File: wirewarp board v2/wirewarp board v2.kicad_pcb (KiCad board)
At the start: 2 copper layers, 1443 parts

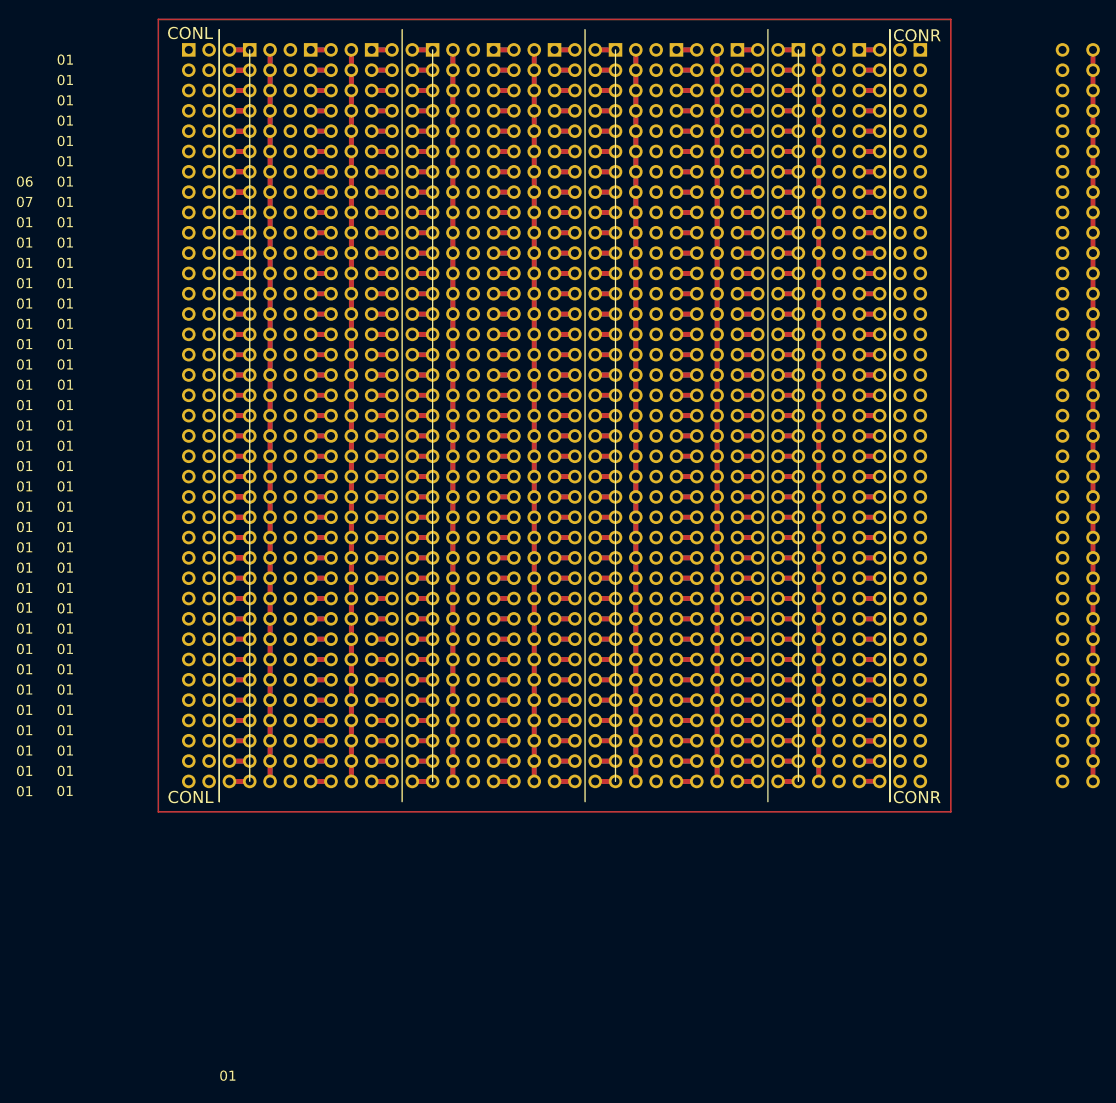
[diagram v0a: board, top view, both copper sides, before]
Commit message: protoboard sketch on kicad
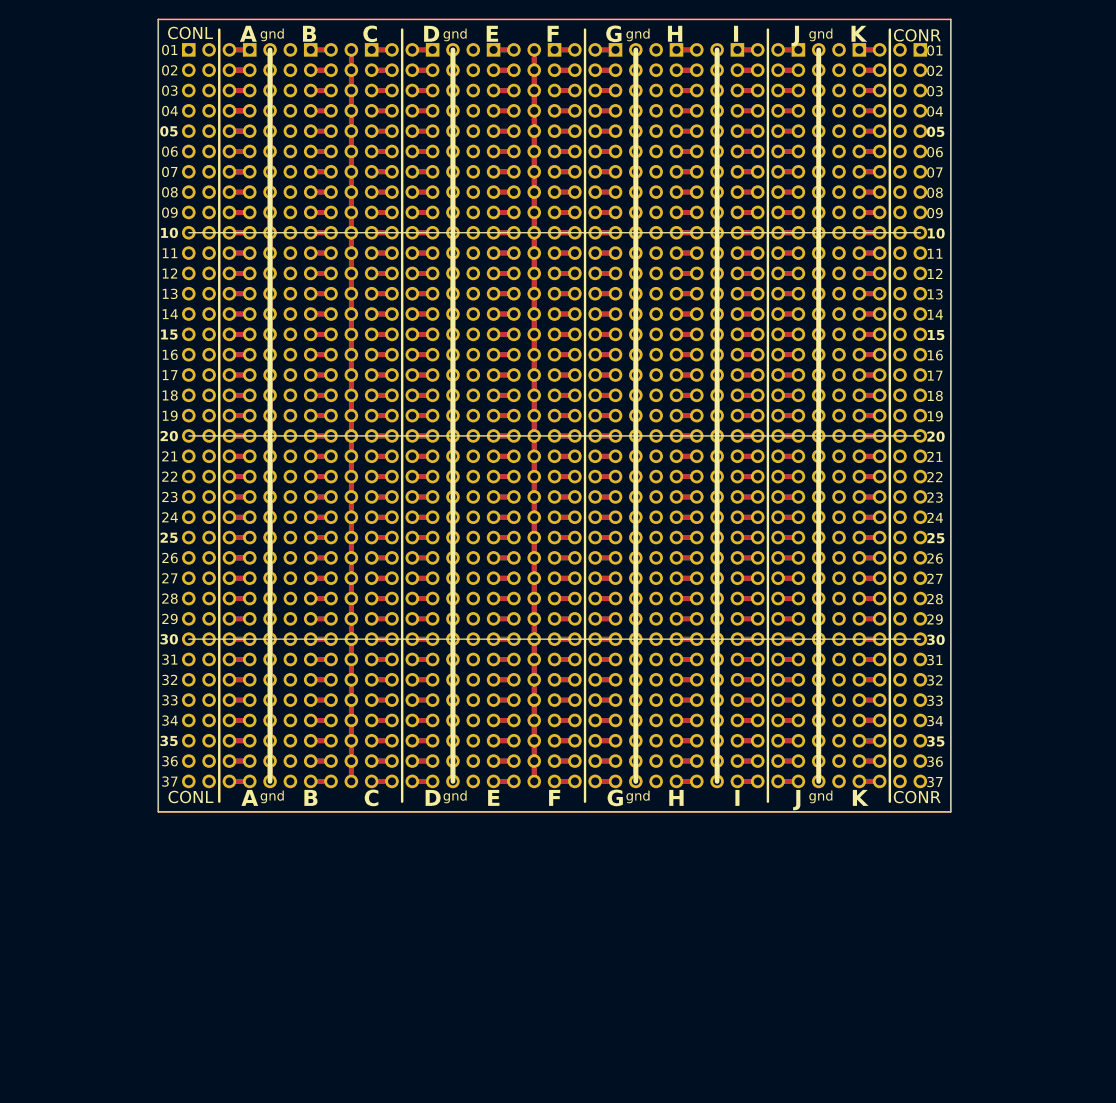
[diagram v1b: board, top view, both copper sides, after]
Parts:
- removed the ? at (167.6, 62.2)
- removed the ? at (163.8, 110.5)
- removed the ? at (167.6, 64.8)
- removed the ? at (163.8, 95.2)
- removed the ? at (167.6, 82.5)
- removed the ? at (167.6, 118.1)
- removed the ? at (163.8, 62.2)
- removed the ? at (163.8, 102.9)
- removed the ? at (163.8, 120.7)
- removed the ? at (167.6, 110.5)
- removed the ? at (167.6, 72.4)
- removed the ? at (163.8, 54.6)
- removed the ? at (163.8, 141.0)
- removed the ? at (163.8, 143.5)
- removed the ? at (167.6, 123.2)
- removed the ? at (167.6, 80.0)
- removed the ? at (167.6, 59.7)
- removed the ? at (167.6, 108.0)
- removed the ? at (167.6, 113.0)
- removed the ? at (163.8, 125.7)
- removed the ? at (163.8, 115.6)
- removed the ? at (167.6, 105.4)
- removed the ? at (163.8, 59.7)
- removed the ? at (167.6, 67.3)
- removed the ? at (163.8, 138.4)
- removed the ? at (167.6, 135.9)
- removed the ? at (167.6, 133.3)
- removed the ? at (167.6, 125.7)
- removed the ? at (167.6, 130.8)
- removed the ? at (163.8, 87.6)
- removed the ? at (163.8, 82.5)
- removed the ? at (163.8, 74.9)
- removed the ? at (163.8, 130.8)
- removed the ? at (167.6, 85.1)
- removed the ? at (167.6, 90.2)
- removed the ? at (163.8, 128.3)
- removed the ? at (163.8, 85.1)
- removed the ? at (167.6, 97.8)
- removed the ? at (163.8, 118.1)
- removed the ? at (167.6, 102.9)
- removed the ? at (163.8, 135.9)
- removed the ? at (167.6, 120.7)
- removed the ? at (163.8, 92.7)
- removed the ? at (167.6, 128.3)
- removed the ? at (163.8, 146.1)
- removed the ? at (167.6, 95.2)
- removed the ? at (167.6, 138.4)
- removed the ? at (167.6, 100.3)
- removed the ? at (167.6, 143.5)
- removed the ? at (163.8, 123.2)
- removed the ? at (167.6, 69.8)
- removed the ? at (167.6, 57.1)
- removed the ? at (167.6, 146.1)
- removed the ? at (163.8, 100.3)
- removed the ? at (167.6, 74.9)
- removed the ? at (167.6, 87.6)
- removed the ? at (163.8, 90.2)
- removed the ? at (167.6, 115.6)
- removed the ? at (163.8, 133.3)
- removed the ? at (163.8, 97.8)
- removed the ? at (163.8, 72.4)
- removed the ? at (163.8, 57.1)
- removed the ? at (167.6, 77.5)
- removed the ? at (163.8, 67.3)
- removed the ? at (167.6, 54.6)
- removed the ? at (163.8, 80.0)
- removed the ? at (163.8, 108.0)
- removed the ? at (163.8, 77.5)
- removed the ? at (167.6, 141.0)
- removed the ? at (163.8, 64.8)
- removed the ? at (163.8, 69.8)
- removed the ? at (163.8, 113.0)
- removed the ? at (167.6, 92.7)
- removed the ? at (163.8, 105.4)
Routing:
- net (no net): track 3477.3 -> 3375.7 mm
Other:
- board outline added: 99.1 x 99.1 mm
- board text added: "gnd"

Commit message: protoboard for wire wrap v2 kicad added
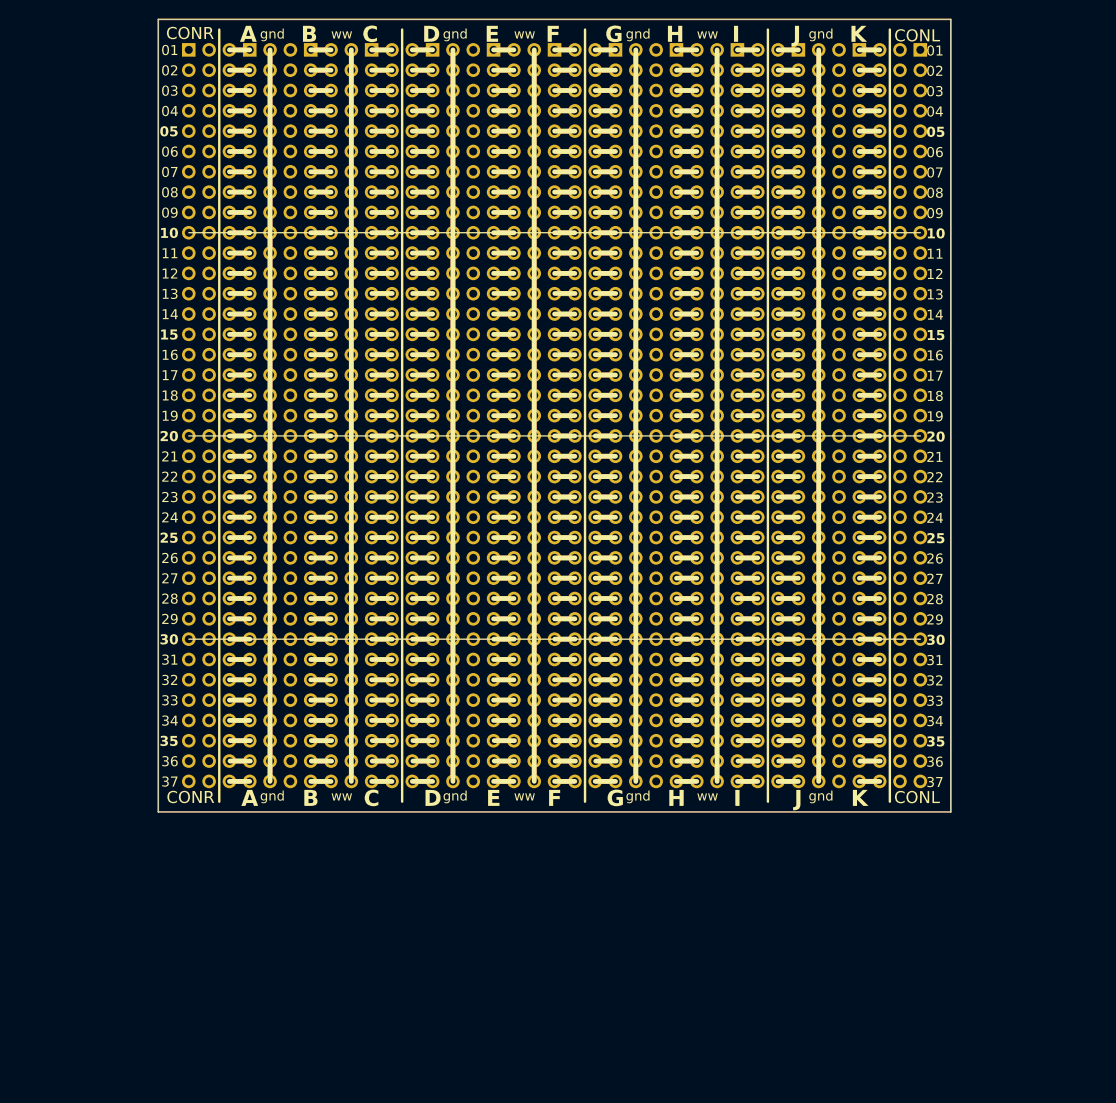
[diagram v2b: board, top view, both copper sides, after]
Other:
- board text added: "sk"
- board text added: "ww"

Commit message: update version 2 of 10x10 protoboard
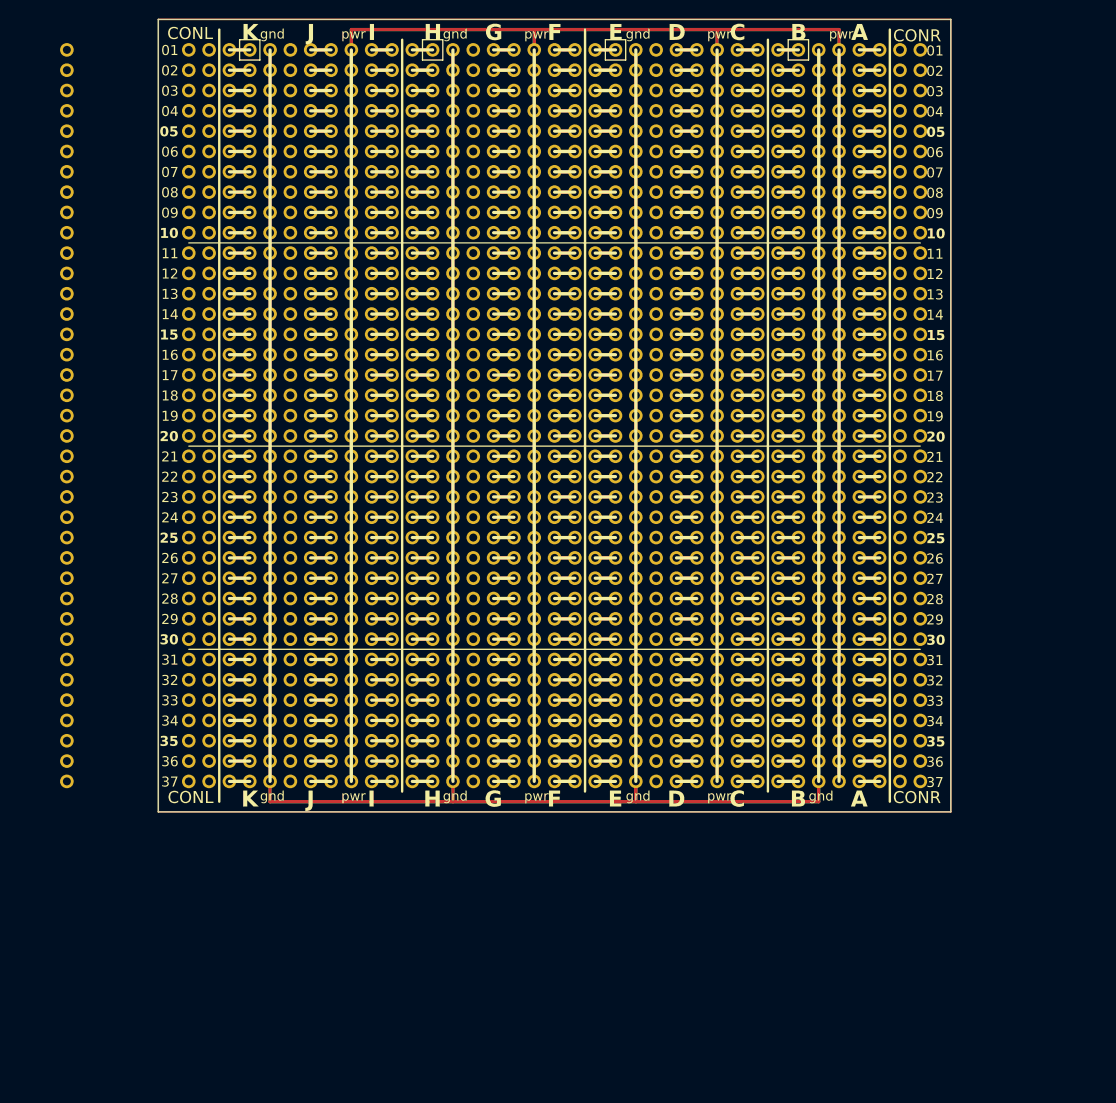
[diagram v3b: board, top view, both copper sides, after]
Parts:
- added ?: , , F.Cu at (64.8, 59.7)
- added ?: , , F.Cu at (64.8, 62.2)
- added ?: , , F.Cu at (64.8, 133.3)
- added ?: , , F.Cu at (64.8, 64.8)
- added ?: , , F.Cu at (64.8, 110.5)
- added ?: , , F.Cu at (64.8, 135.9)
- added ?: , , F.Cu at (64.8, 95.2)
- added ?: , , F.Cu at (64.8, 97.8)
- added ?: , , F.Cu at (64.8, 90.2)
- added ?: , , F.Cu at (64.8, 141.0)
- added ?: , , F.Cu at (64.8, 67.3)
- added ?: , , F.Cu at (64.8, 82.5)
- added ?: , , F.Cu at (64.8, 87.6)
- added ?: , , F.Cu at (64.8, 115.6)
- added ?: , , F.Cu at (64.8, 92.7)
- added ?: , , F.Cu at (64.8, 74.9)
- added ?: , , F.Cu at (64.8, 54.6)
- added ?: , , F.Cu at (64.8, 143.5)
- added ?: , , F.Cu at (64.8, 130.8)
- added ?: , , F.Cu at (64.8, 113.0)
- added ?: , , F.Cu at (64.8, 72.4)
- added ?: , , F.Cu at (64.8, 102.9)
- added ?: , , F.Cu at (64.8, 138.4)
- added ?: , , F.Cu at (64.8, 108.0)
- added ?: , , F.Cu at (64.8, 123.2)
- added ?: , , F.Cu at (64.8, 128.3)
- added ?: , , F.Cu at (64.8, 77.5)
- added ?: , , F.Cu at (64.8, 85.1)
- added ?: , , F.Cu at (64.8, 69.8)
- added ?: , , F.Cu at (64.8, 125.7)
- added ?: , , F.Cu at (64.8, 105.4)
- added ?: , , F.Cu at (64.8, 80.0)
- added ?: , , F.Cu at (64.8, 100.3)
- added ?: , , F.Cu at (64.8, 146.1)
- added ?: , , F.Cu at (64.8, 120.7)
- added ?: , , F.Cu at (64.8, 118.1)
- added ?: , , F.Cu at (64.8, 57.1)
- moved ? 25.4 mm to (39.4, 143.5)
- moved ? 25.4 mm to (39.4, 125.7)
- moved ? 25.4 mm to (39.4, 64.8)
- moved ? 25.4 mm to (39.4, 92.7)
- moved ? 25.4 mm to (39.4, 77.5)
- moved ? 25.4 mm to (39.4, 87.6)
- moved ? 25.4 mm to (39.4, 146.1)
- moved ? 25.4 mm to (39.4, 128.3)
- moved ? 25.4 mm to (39.4, 74.9)
- moved ? 25.4 mm to (39.4, 97.8)
- moved ? 25.4 mm to (39.4, 135.9)
- moved ? 25.4 mm to (39.4, 110.5)
- moved ? 25.4 mm to (39.4, 85.1)
- moved ? 25.4 mm to (39.4, 72.4)
- moved ? 25.4 mm to (39.4, 59.7)
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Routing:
- net (no net): track 3375.7 -> 3830.3 mm
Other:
- board text added: "pwr"
- board text removed: "sk"
- board text removed: "ww"

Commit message: update of 10x10 protoboards, conn connected
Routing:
- net (no net): track 3830.3 -> 4206.2 mm
